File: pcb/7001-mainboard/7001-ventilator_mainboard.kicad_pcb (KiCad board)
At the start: 2 copper layers, 99 x 110.5 mm, 165 parts, among them J1 USB_B_Micro, J10 6-pin header, J11 2-pin screw terminal, J13 2-pin screw terminal, J14 2-pin screw terminal, J15 2x10-pin header, J16 10-pin SWD header, J2 6-pin FFC connector, J3 2-pin screw terminal, J4 2-pin screw terminal, J5 2-pin screw terminal, J6 5V out, J7 6-pin FFC connector, J8 2-pin screw terminal, J9 Raspberry_Pi_2_3, Q1 NX3020NAKV,115, U1 MPRLS0001PG0000SA, U11 MPVZ5010GW6U, U13 ITS4142NHUMA1, U14 ITS4142NHUMA1, U15 MCP4725, U16 LD1086DT33TR, U2 TPD2E2U06, U3 LPC11U37FBD48-401_, U4 MCP1825S-3302E, U5 S24SE05004PDFA_DC-DC, U6 MCP4725, U7 ITS4142NHUMA1, U8 MPRLS0001PG0000SA, U9 ABPDXXX000XXAX5, Y1 12MHz

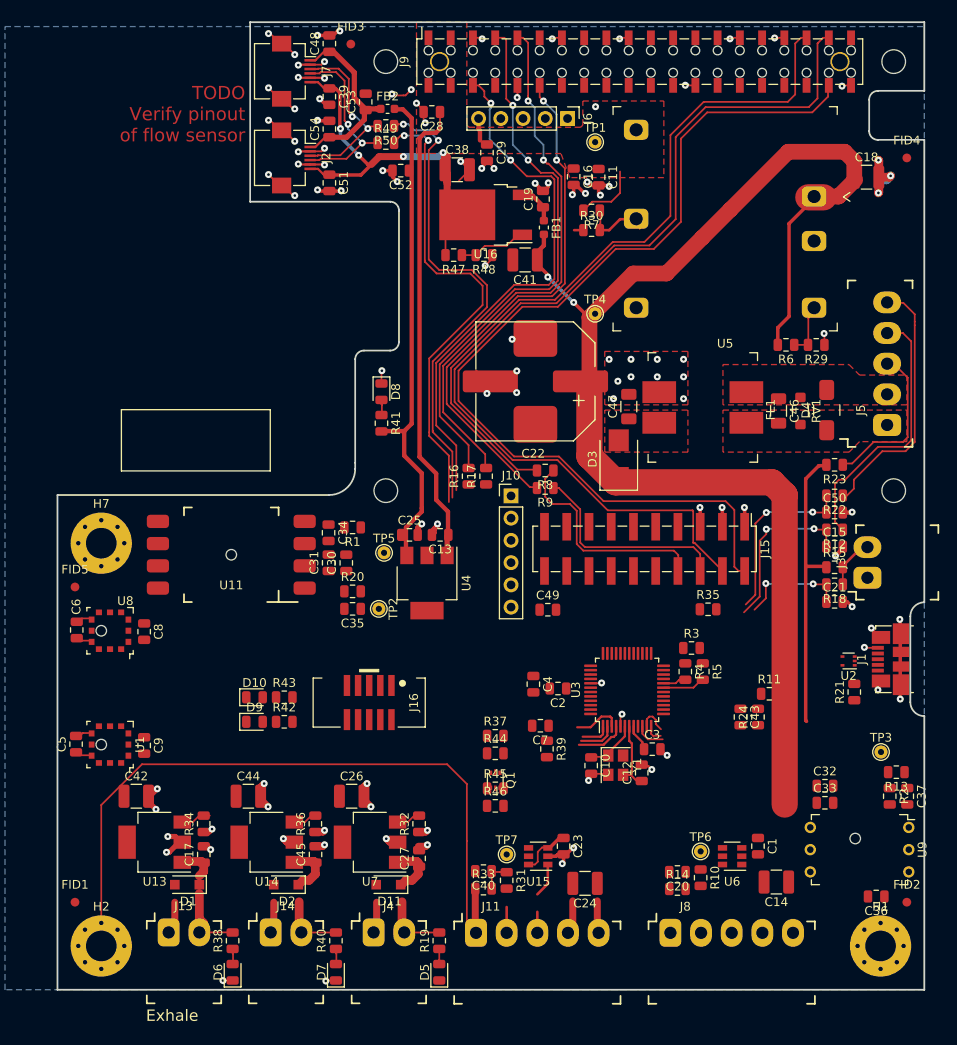
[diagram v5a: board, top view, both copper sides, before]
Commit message: PCB layout: DRC pass
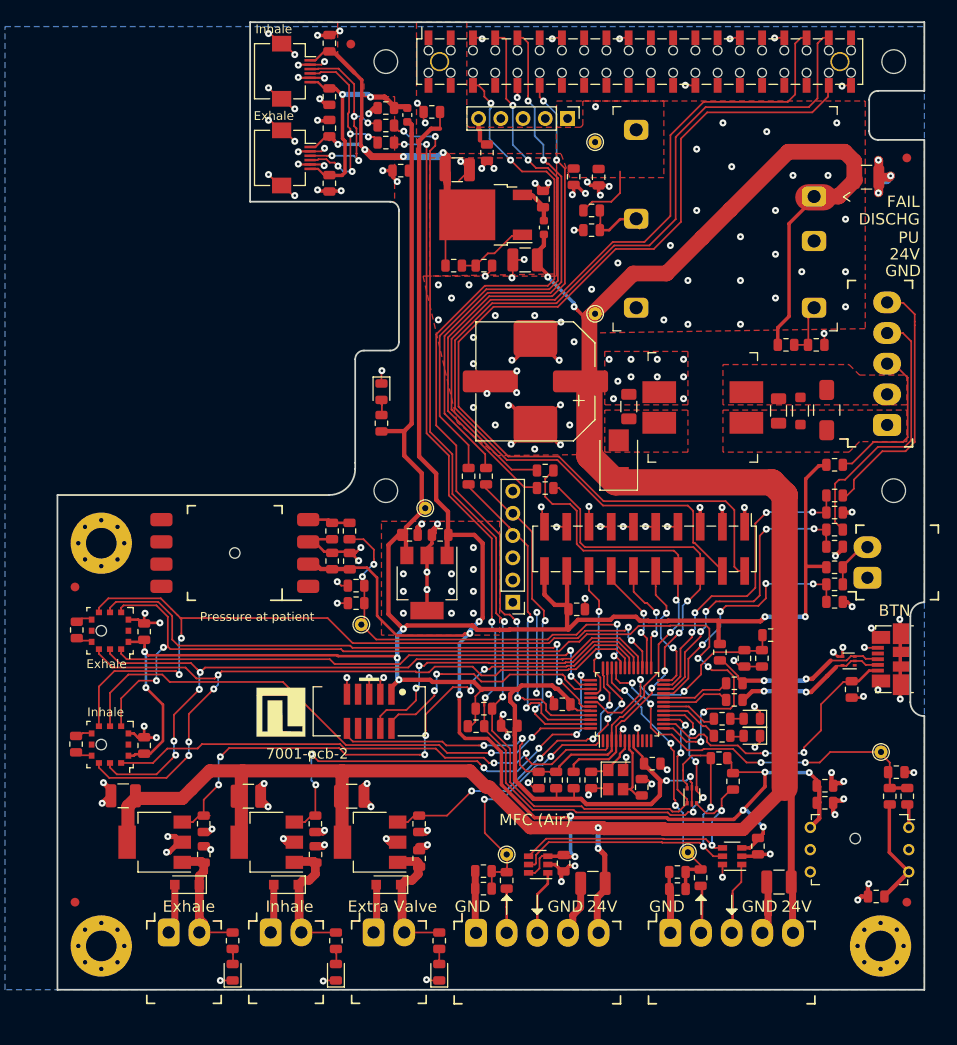
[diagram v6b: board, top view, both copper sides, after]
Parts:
- added LOGO1: LOGO, Jitter_Logos:JitterLogo, F.Cu at (91.0, 178.4)
- J11, J8: value 2-pin screw terminal -> 5-pin screw terminal
- J5: value 2-pin screw terminal -> 5-pin screw terminal vertical
- U16: value LD1086DT33TR -> LD1086DTTR
- moved D10 57.0 mm to (145.3, 181.0), turned to 180 degrees
- moved D9 56.8 mm to (145.3, 179.1), turned to 180 degrees
- moved R43 50.2 mm to (141.9, 181.0), turned to 180 degrees
- moved R42 50.0 mm to (141.9, 179.1), turned to 180 degrees
- moved R46 27.3 mm to (143.2, 186.2), turned to 90 degrees
- moved R45 25.8 mm to (141.6, 183.6)
- moved R35 24.8 mm to (125.0, 186.1), turned to 270 degrees
- moved Q1 22.5 mm to (138.4, 187.8), turned to 90 degrees
- moved J10 12.2 mm to (118.0, 165.8), turned to 180 degrees
- moved TP5 6.94 mm to (108.0, 155.0)
- moved C43 6.72 mm to (144.4, 172.2)
- moved R24 6.72 mm to (146.4, 172.2)
- moved R11 6.70 mm to (147.4, 169.5)
- moved C51 6.25 mm to (97.0, 111.6), turned to 90 degrees
- moved C7 6.20 mm to (121.0, 186.1), turned to 270 degrees
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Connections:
- J2 pad 1: /V_flow_3v3 -> /V_flow_heater
- J2 pad 3: /FLOW_I2C_SDA -> /FLOW_I2C_SCL
- J2 pad 4: /FLOW_I2C_SCL -> /FLOW_I2C_SDA
- J2 pad 6: /V_flow_heater -> /V_flow_3v3
- J7 pad 1: /V_flow_3v3 -> /V_flow_heater
- J7 pad 3: /FLOW_I2C_SDA -> /FLOW_I2C_SCL
- J7 pad 4: /FLOW_I2C_SCL -> /FLOW_I2C_SDA
- J7 pad 6: /V_flow_heater -> /V_flow_3v3
- U3 pad 1: /PSENSE_1_DATA_READY -> (no net)
- U3 pad 10: /LED_STATUS -> (no net)
- U3 pad 11: /USER_SWITCH -> (no net)
- U3 pad 12: /POWER_STATUS_FAIL -> (no net)
- U3 pad 13: /POWER_STATUS_DISCHARGING -> /PSENSE_RESET
- U3 pad 18: /PSENSE_2_DATA_READY -> /LED_STATUS
- U3 pad 21: (no net) -> /USER_SWITCH
- U3 pad 22: (no net) -> /POWER_STATUS_DISCHARGING
- U3 pad 23: /PSENSE_2_SPI_~CS~ -> /POWER_STATUS_FAIL
- U3 pad 24: /PSENSE_RESET -> /MCU_IO_4
- U3 pad 25: (no net) -> /MCU_IO_3
- U3 pad 26: (no net) -> /MCU_IO_2
- U3 pad 34: /A_MFC_FEEDBACK_AIR -> /A_MFC_FEEDBACK_O2
- U3 pad 35: /A_MFC_FEEDBACK_O2 -> /A_MFC_FEEDBACK_AIR
- U3 pad 38: /MCU_IO_3 -> /PSENSE_2_SPI_~CS~
- U3 pad 43: /MCU_IO_4 -> /PSENSE_2_DATA_READY
- U3 pad 48: /MCU_IO_2 -> /PSENSE_1_DATA_READY
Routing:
- net +3V3: track 92.9 -> 285.3 mm, vias 0 -> 9
- net +5V: track 69.7 -> 199.1 mm, vias 0 -> 9
- net +24V: track 155.9 -> 281.5 mm, vias 2 -> 4
- net /PSENSE_RESET: track 0.00 -> 110.4 mm, vias 0 -> 6
- net /PSENSE_SPI_MISO: track 0.00 -> 91.5 mm, vias 0 -> 4
- net /PSENSE_SPI_CLK: track 0.00 -> 88.6 mm, vias 0 -> 4
- net /PSENSE_SPI_MOSI: track 0.00 -> 85.7 mm, vias 0 -> 4
- net GND: track 256.0 -> 332.6 mm, vias 105 -> 205
- net /I2C_3V3_SDA: track 55.2 -> 120.8 mm, vias 2 -> 8
- net /EXHALE_PWM: track 3.03 -> 68.7 mm, vias 0 -> 6
- net /PSENSE_2_DATA_READY: track 0.00 -> 65.1 mm, vias 0 -> 2
- net /I2C_3V3_SCL: track 54.6 -> 119.3 mm, vias 2 -> 6
- net /PSENSE_1_DATA_READY: track 3.35 -> 64.5 mm, vias 0 -> 2
- net /PSENSE_2_SPI_~CS~: track 0.00 -> 58.7 mm, vias 0 -> 2
- net /~RESET~: track 30.8 -> 87.4 mm, vias 0 -> 4
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- added copper zone on F.Cu, net /V_flow_heater
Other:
- board text added: "24V"
- board text added: "7001-pcb-2"
- board text added: "BTN"
- board text added: "DISCHG"
- board text added: "Extra Valve"
- board text added: "FAIL"
- board text added: "GND"
- board text added: "Inhale"
- board text added: "MFC (Air)"
- board text added: "PU"
- board text added: "Pressure at patient"
- board text removed: "TODO Verify pinout of flow sensor"

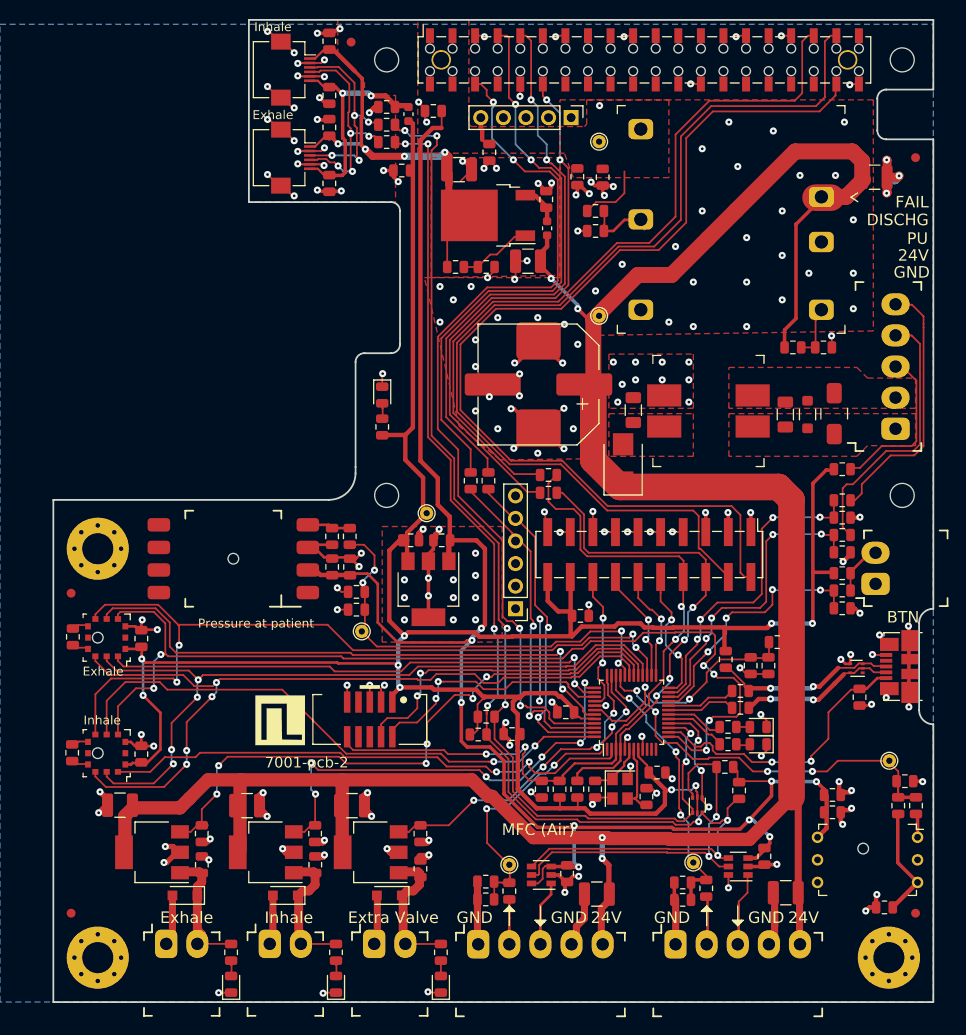
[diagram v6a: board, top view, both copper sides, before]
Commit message: PCB: improve silkscreen, mounting holes
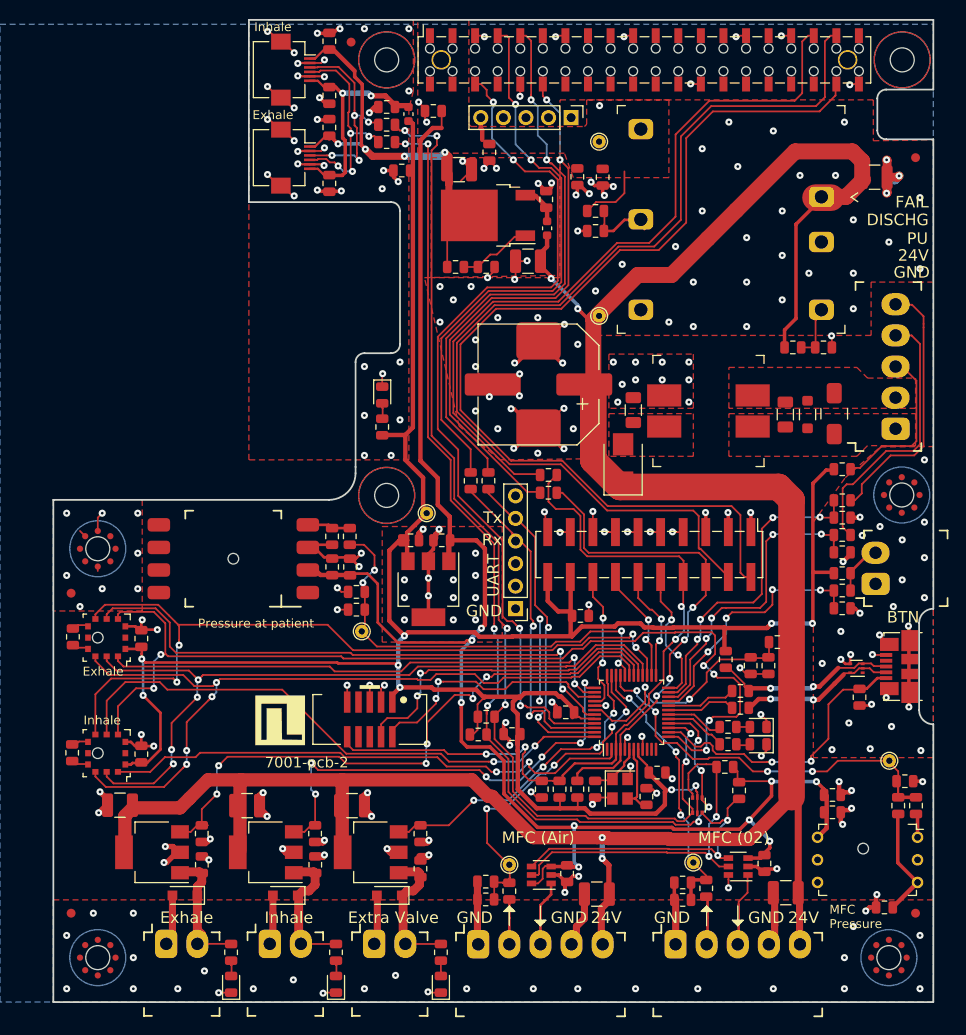
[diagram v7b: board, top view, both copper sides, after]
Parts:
- H1, H2, H7: footprint MountingHole:MountingHole_3.5mm_Pad_Via -> Jitter_Footprints:MountingHole_2.7mm_M2.5_Pad__wavesolder
- H3: footprint MountingHole:MountingHole_2.7mm_M2.5 -> Jitter_Footprints:MountingHole_2.7mm_M2.5_Pad__wavesolder
- H4, H5, H6: footprint MountingHole:MountingHole_2.7mm_M2.5 -> Jitter_Footprints:MountingHole_2.7mm_M2.5__wavesolder
- moved C1 0.80 mm to (146.0, 194.4)
- moved H3 0.07 mm to (161.4, 152.9)
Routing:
- net GND: track 332.6 -> 335.9 mm, vias 205 -> 265
- net /USB_VBUS: track 32.4 -> 33.0 mm
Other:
- board text added: "MFC (02)"
- board text added: "MFC Pressure"
- board text added: "Rx"
- board text added: "Tx"
- board text added: "UART"

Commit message: PCB: minor improvements, add OperationAir logo
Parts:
- added LOGO2: LOGO, OperationAir:OperationAir260, F.Cu at (110.5, 171.6)
- moved C29 1.27 mm to (115.0, 115.7)
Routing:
- net +5V: track 198.9 -> 201.7 mm
- net /EXHALE_PWM: track 68.7 -> 69.6 mm
- net /A_MFC_FEEDBACK_AIR: track 39.5 -> 38.5 mm
- net GND: vias 265 -> 308
- added copper zone on F.Cu, net +24V
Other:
- board text added: "+"
- board text added: "-"
- board text added: "RPI Dispay"
